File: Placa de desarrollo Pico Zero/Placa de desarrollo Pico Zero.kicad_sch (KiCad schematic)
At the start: 33 parts, among them J1 LEFT-MALE, J2 RIGHT-MALE, J3 DOWN-MALE, J4 DOWN-FEMALE, J5 LEFT-FEMALE, J6 RIGHT-FEMALE, J7 USB_A, U1 RP2040

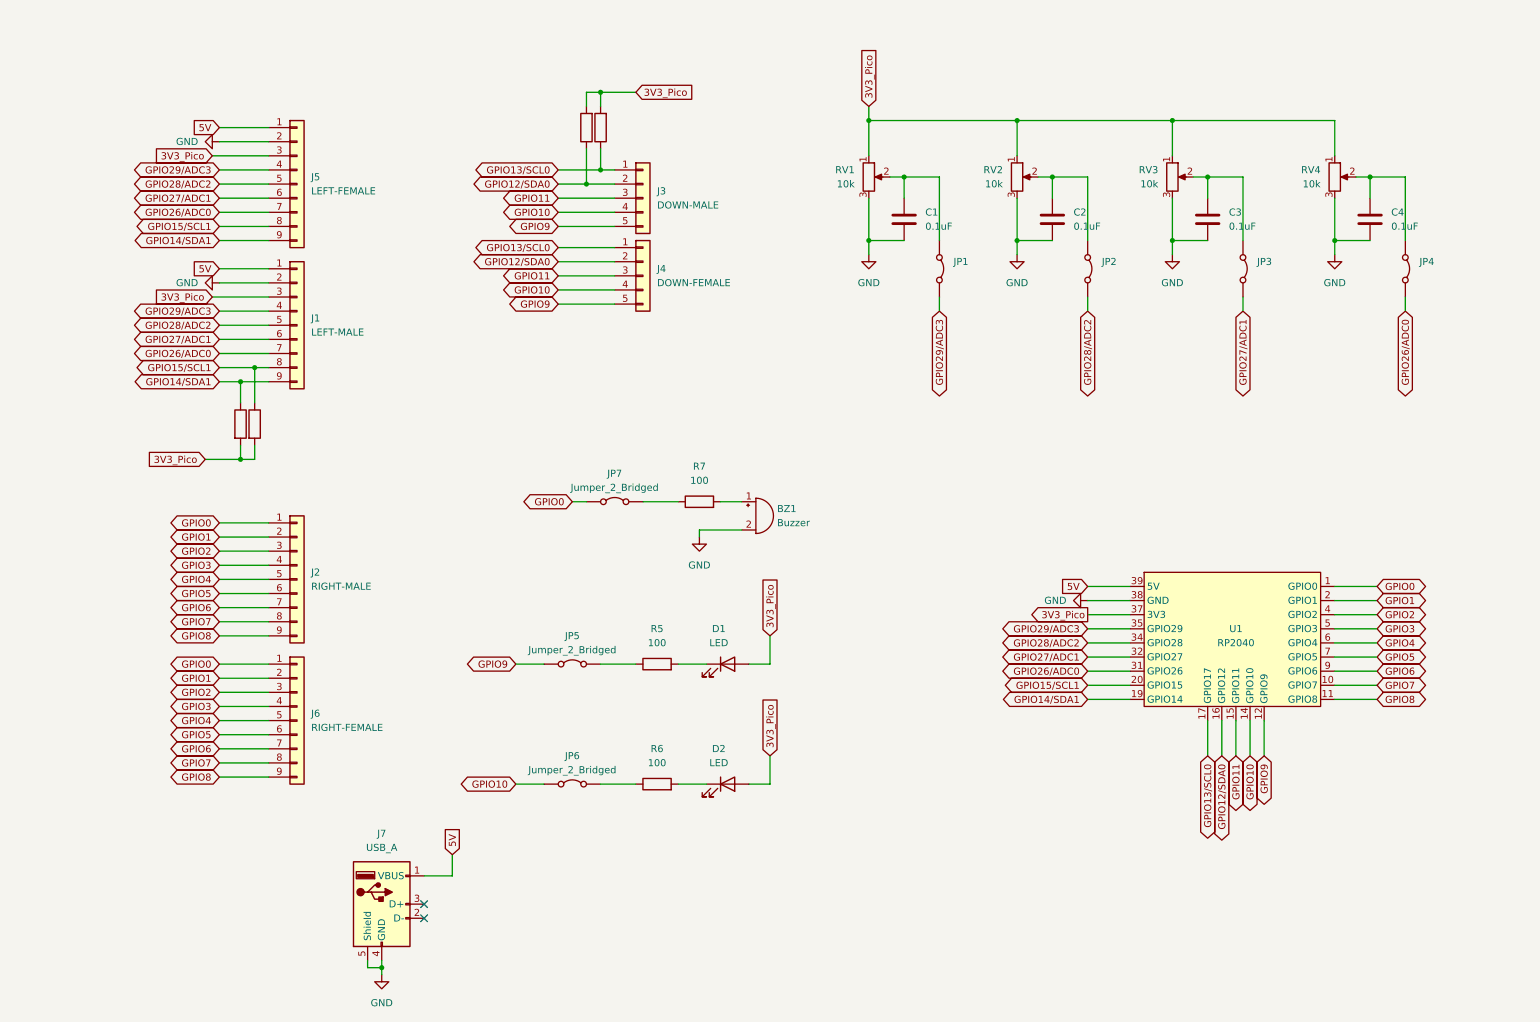
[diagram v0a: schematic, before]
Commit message: Version 1.0 de la placa de desarrollor para la Pico Zero
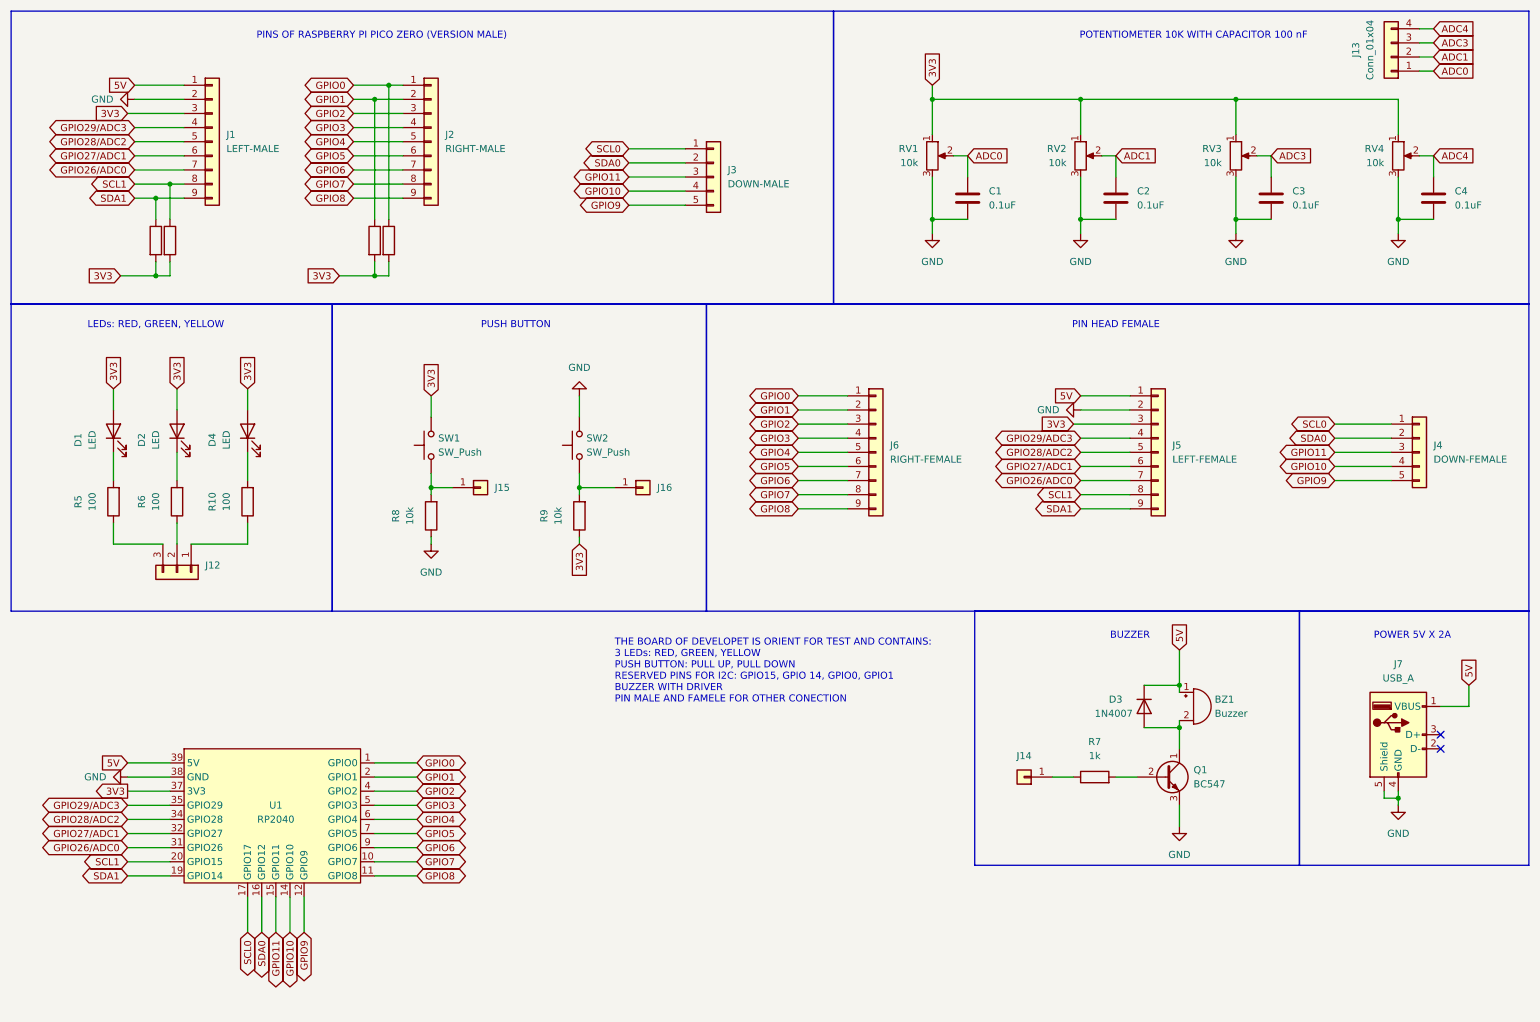
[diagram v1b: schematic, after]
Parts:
- removed JP1, JP2, JP3, JP4, JP5, JP6, JP7: Jumper_2_Bridged, Connector_PinHeader_2.54mm:PinHeader_1x02_P2.54mm_Vertical, symbol Jumper:Jumper_2_Bridged
- added D3: 1N4007, Diode_THT:D_DO-41_SOD81_P10.16mm_Horizontal, symbol Diode:1N4007
- added D4: LED, LED_THT:LED_D5.0mm, symbol Device:LED
- added J12: Conn_01x03, Connector_PinHeader_2.54mm:PinHeader_1x03_P2.54mm_Vertical, symbol Connector_Generic:Conn_01x03
- added J13: Conn_01x04, Connector_PinHeader_2.54mm:PinHeader_1x04_P2.54mm_Vertical, symbol Connector_Generic:Conn_01x04
- added J14, J15, J16: Conn_01x01, Connector_PinHeader_2.54mm:PinHeader_1x01_P2.54mm_Vertical, symbol Connector_Generic:Conn_01x01
- added Q1: BC547, Package_TO_SOT_THT:TO-92_Inline, symbol Transistor_BJT:BC547
- added R10: 100, Resistor_THT:R_Axial_DIN0207_L6.3mm_D2.5mm_P10.16mm_Horizontal, symbol Device:R
- added R8, R9: 10k, Resistor_THT:R_Axial_DIN0207_L6.3mm_D2.5mm_P10.16mm_Horizontal, symbol Device:R
- added SW1, SW2: SW_Push, Button_Switch_THT:SW_Tactile_Straight_KSL0Axx1LFTR, symbol Switch:SW_Push
- R7: value 100 -> 1k
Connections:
- net 5V: now also BZ1.1 (+), D3.1 (K)
- net GND: now also Q1.3 (E), R8.1, SW2.2; no longer BZ1.2 (-)
- net GPIO0: now also R4.1
- net GPIO1: now also R3.1
- net ADC3: now reaches C3.1, RV3.2
- net ADC3: now also J13.3 (Pin_3)
- net ADC1: now reaches C2.1, RV2.2
- net ADC1: now also J13.2 (Pin_2)
- net at R5.1: now also J12.3 (Pin_3)
- net ADC4: now reaches C4.1, RV4.2
- net ADC4: now also J13.4 (Pin_4)
- net ADC0: now reaches C1.1, RV1.2
- net ADC0: now also J13.1 (Pin_1)
- net at R7.2: now also Q1.2 (B); no longer BZ1.1 (+)
- net at R7.1: now also J14.1 (Pin_1)
- net at R6.1: now also J12.2 (Pin_2)
- net 3V3_Pico renamed 3V3
- net 3V3: now also D4.2 (A), R9.1, SW1.2
- net GPIO12/SDA0 renamed SDA0
- net SDA0: no longer R4.1
- net GPIO13/SCL0 renamed SCL0
- net SCL0: no longer R3.1
- net GPIO14/SDA1 renamed SDA1
- net GPIO15/SCL1 renamed SCL1
- new net: J15.1 (Pin_1), R8.2, SW1.1
- new net: BZ1.2 (-), D3.2 (A), Q1.1 (C)
- new net: J12.1 (Pin_1), R10.1
- new net: J16.1 (Pin_1), R9.2, SW2.1
- new net: D4.1 (K), R10.2
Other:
- note added: "BUZZER"
- note added: "LEDs: RED, GREEN, YELLOW"
- note added: "PIN HEAD FEMALE"
- note added: "PINS OF RASPBERRY PI PICO ZERO (VERSION MALE)"
- note added: "POTENTIOMETER 10K WITH CAPACITOR 100 nF"
- note added: "POWER 5V X 2A"
- note added: "PUSH BUTTON"
- note added: "THE BOARD OF DEVELOPET IS ORIENT FOR TEST AND CONTAINS: 3 LEDs: RED, GREEN, YELLOW PUSH BUTTON: PULL UP, PULL DOWN RESERVED PINS FOR I2C: GPIO15, GPIO 14, GPIO0, GPIO1 BUZZER WITH DRIVER PIN MALE AND FAMELE FOR OTHER CONECTION"
- moved on the sheet: BZ1, C1, C2, C3, C4, D1, D2, J1, J2, J3, J4, J5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
